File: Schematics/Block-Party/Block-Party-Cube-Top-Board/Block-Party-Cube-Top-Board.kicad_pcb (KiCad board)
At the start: 2 copper layers, 50 x 50 mm, 5 parts

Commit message: Revision 1.01 of the PCBs
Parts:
- removed J3, J4, J5: ~, Connector_PinHeader_2.54mm:PinHeader_1x01_P2.54mm_Vertical
- J2: value ~ -> 4328; footprint Connector_PinHeader_2.54mm:PinHeader_1x01_P2.54mm_Vertical -> adafruit-jst-4328:ADAFRUIT_4328; moved to B.Cu
- moved J2 15.7 mm to (140.3, 101.0), turned to 180 degrees
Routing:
- net +5V: track 13.5 -> 9.74 mm, vias 0 -> 1
- net Net-(J1-DOUT): track 13.5 -> 9.88 mm, vias 0 -> 1
- net Net-(J1-SIG): track 13.5 -> 14.0 mm, vias 0 -> 1
- net GND: vias 0 -> 1
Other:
- outline, holes or cut-outs redrawn

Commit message: Found a good jst part number and updated the BOMs
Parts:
- J2: value 4328 -> BM04B-SRSS-TB(LF)(SN)
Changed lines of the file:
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@@
 			)
 		)
+		(sheetname "Root")
+		(sheetfile "Block-Party-Cube-Top-Board.kicad_sch")
 		(attr through_hole)
 		(fp_rect
@@
 			)
 		)
-		(property "Value" "4328"
+		(property "Value" "BM04B-SRSS-TB(LF)(SN) "
 			(at 4.605 -4.435 180)
 			(layer "B.Fab")
@@
 			)
 		)
-		(property "Description" ""
+		(property "Description" "BM04B-SRSS-TB(LF)(SN) "
 			(at 0 0 0)
 			(unlocked yes)
@@
 			)
 		)
-		(property "MANUFACTURER" "Adafruit"
-			(at 0 0 0)
-			(unlocked yes)
-			(layer "B.Fab")
-			(hide yes)
-			(effects
-				(font
-					(size 1 1)
-					(thickness 0.15)
-				)
-				(justify mirror)
-			)
-		)
+		(property "MANUFACTURER" "JST"
+			(at 0 0 0)
+			(unlocked yes)
+			(layer "B.Fab")
+			(hide yes)
+			(effects
+				(font
+					(size 1 1)
+					(thickness 0.15)
+				)
+				(justify mirror)
+			)
+		)
+		(sheetname "Root")
+		(sheetfile "Block-Party-Cube-Top-Board.kicad_sch")
 		(attr smd)
 		(fp_line

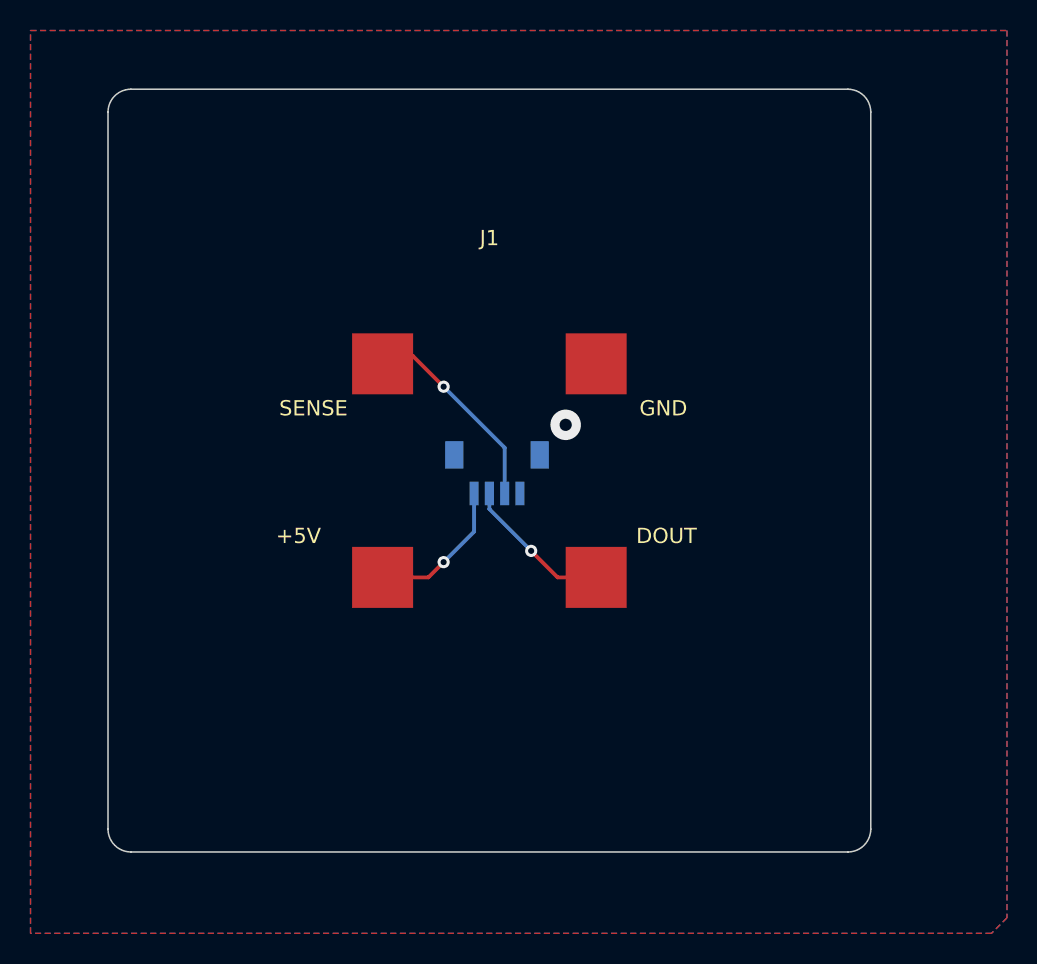
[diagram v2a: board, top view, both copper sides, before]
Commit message: Made the top and bottom PCB the same size
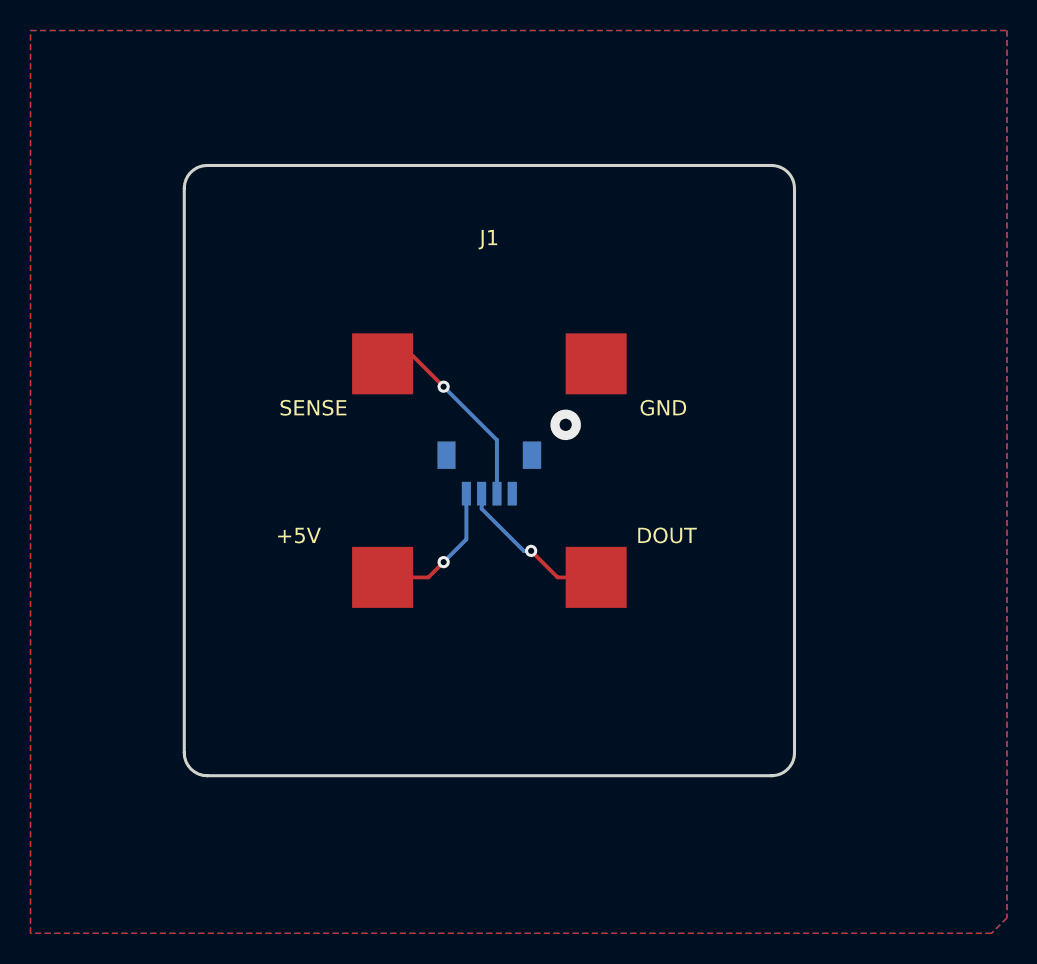
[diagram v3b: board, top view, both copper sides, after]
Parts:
- moved J2 0.51 mm to (139.8, 101.0)
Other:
- board size 50 x 50 mm -> 40 x 40 mm
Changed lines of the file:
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@@
 	(footprint "adafruit-jst-4328:ADAFRUIT_4328"
 		(layer "B.Cu")
-		(at 140.308 100.963 180)
+		(at 139.8 100.9755 180)
 		(property "Reference" "J2"
 			(at -0.475 3.535 180)
@@
 	)
 	(gr_line
-		(start 114.808 124.738)
-		(end 114.808 77.738)
-		(stroke
-			(width 0.1)
+		(start 159.808 82.738)
+		(end 159.808 119.738)
+		(stroke
+			(width 0.2)
 			(type default)
 		)
@@
 	)
 	(gr_arc
-		(start 163.308 76.238)
-		(mid 164.36866 76.67734)
-		(end 164.808 77.738)
-		(stroke
-			(width 0.1)
+		(start 159.808 119.738)
+		(mid 159.36866 120.79866)
+		(end 158.308 121.238)
+		(stroke
+			(width 0.2)
+			(type default)
+		)
+		(layer "Edge.Cuts")
+	)
+	(gr_line
+		(start 121.308 81.238)
+		(end 158.308 81.238)
+		(stroke
+			(width 0.2)
+			(type default)
+		)
+		(layer "Edge.Cuts")
+	)
+	(gr_line
+		(start 158.308 121.238)
+		(end 121.308 121.238)
+		(stroke
+			(width 0.2)
+			(type default)
+		)
+		(layer "Edge.Cuts")
+	)
+	(gr_line
+		(start 119.808 119.738)
+		(end 119.808 82.738)
+		(stroke
+			(width 0.2)
 			(type default)
 		)
@@
 	)
 	(gr_arc
-		(start 164.808 124.738)
-		(mid 164.36866 125.79866)
-		(end 163.308 126.238)
-		(stroke
-			(width 0.1)
-			(type default)
-		)
-		(layer "Edge.Cuts")
-	)
-	(gr_line
-		(start 163.308 126.238)
-		(end 116.308 126.238)
-		(stroke
-			(width 0.1)
+		(start 121.308 121.238)
+		(mid 120.24734 120.79866)
+		(end 119.808 119.738)
+		(stroke
+			(width 0.2)
 			(type default)
 		)
@@
 	)
 	(gr_arc
-		(start 116.308 126.238)
-		(mid 115.24734 125.79866)
-		(end 114.808 124.738)
-		(stroke
-			(width 0.1)
+		(start 119.808 82.738)
+		(mid 120.24734 81.67734)
+		(end 121.308 81.238)
+		(stroke
+			(width 0.2)
 			(type default)
 		)
@@
 	)
 	(gr_arc
-		(start 114.808 77.738)
-		(mid 115.24734 76.67734)
-		(end 116.308 76.238)
-		(stroke
-			(width 0.1)
-			(type default)
-		)
-		(layer "Edge.Cuts")
-	)
-	(gr_line
-		(start 164.808 77.738)
-		(end 164.808 124.738)
-		(stroke
-			(width 0.1)
-			(type default)
-		)
-		(layer "Edge.Cuts")
-	)
-	(gr_line
-		(start 116.308 76.238)
-		(end 163.308 76.238)
-		(stroke
-			(width 0.1)
+		(start 158.308 81.238)
+		(mid 159.36866 81.67734)
+		(end 159.808 82.738)
+		(stroke
+			(width 0.2)
 			(type default)
 		)
@@
 	)
 	(segment
+		(start 140.3 99.23)
+		(end 140.3 102.7505)
+		(width 0.25)
+		(layer "B.Cu")
+		(net 2)
+	)
+	(segment
 		(start 136.808 95.738)
-		(end 140.808 99.738)
-		(width 0.25)
-		(layer "B.Cu")
-		(net 2)
-	)
-	(segment
-		(start 140.808 99.738)
-		(end 140.808 102.738)
+		(end 140.3 99.23)
 		(width 0.25)
 		(layer "B.Cu")
@@
 	)
 	(segment
+		(start 139.3 103.7425)
+		(end 139.3 102.7505)
+		(width 0.25)
+		(layer "B.Cu")
+		(net 3)
+	)
+	(segment
 		(start 142.5455 106.5005)
-		(end 139.808 103.763)
+		(end 142.058 106.5005)
 		(width 0.25)
 		(layer "B.Cu")
@@
 	)
 	(segment
-		(start 139.808 103.763)
-		(end 139.808 102.738)
+		(start 142.058 106.5005)
+		(end 139.3 103.7425)
 		(width 0.25)
 		(layer "B.Cu")
@@
 	)
 	(segment
+		(start 138.3 105.746)
+		(end 138.3 102.7505)
+		(width 0.25)
+		(layer "B.Cu")
+		(net 4)
+	)
+	(segment
 		(start 136.808 107.238)
-		(end 138.808 105.238)
-		(width 0.25)
-		(layer "B.Cu")
-		(net 4)
-	)
-	(segment
-		(start 138.808 105.238)
-		(end 138.808 102.738)
-		(width 0.25)
-		(layer "B.Cu")
+		(end 138.3 105.746)
+		(width 0.25)
+		(layer "B.Cu")
